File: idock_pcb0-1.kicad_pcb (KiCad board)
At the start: 2 copper layers, 8 parts, among them J1 entrada, U1 ATmega32A-PU, Y1 8mhz

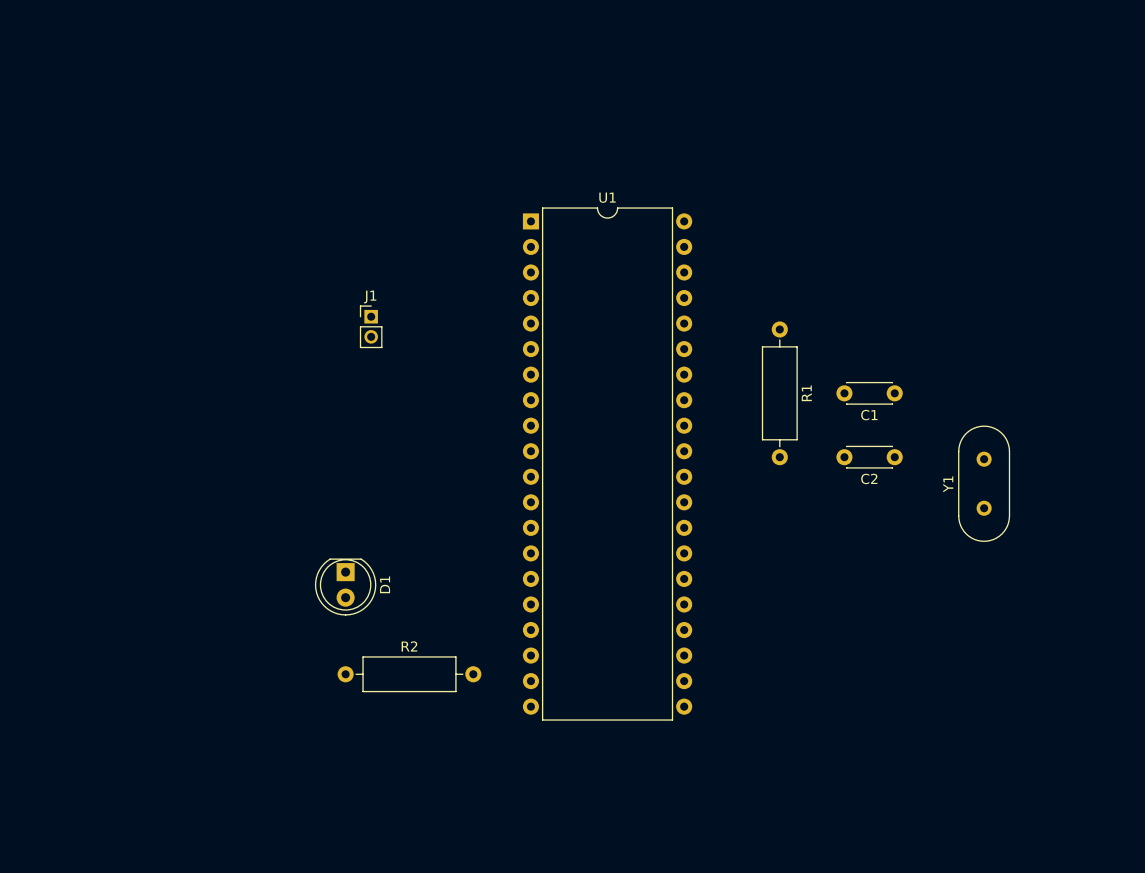
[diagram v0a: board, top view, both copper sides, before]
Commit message: add conections to ipod pcb
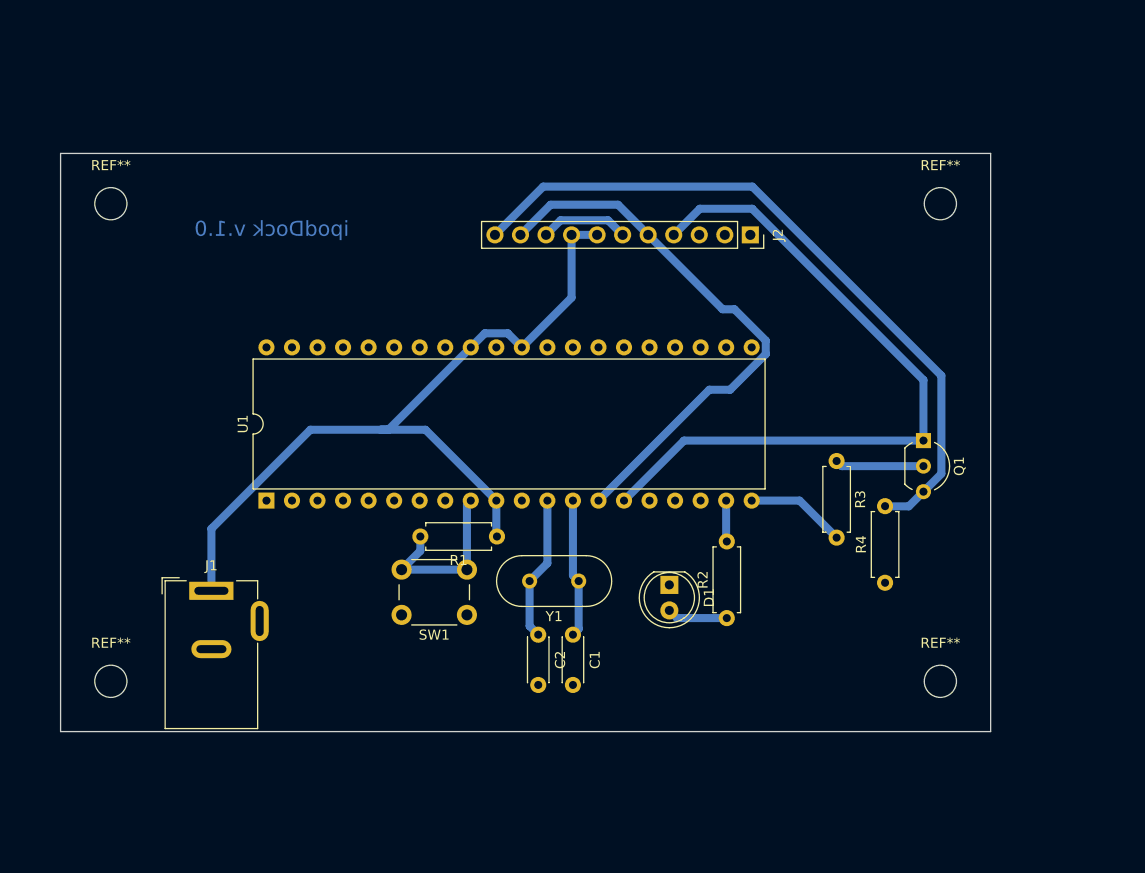
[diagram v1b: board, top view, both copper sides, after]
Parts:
- added J2: bluetooth-dock, Connector_PinSocket_2.54mm:PinSocket_1x11_P2.54mm_Vertical, F.Cu at (173.6, 70.6)
- added Q1: BC548, Package_TO_SOT_THT:TO-92_Inline_Wide, F.Cu at (190.8, 91.1)
- added R3: 10k, Resistor_THT:R_Axial_DIN0207_L6.3mm_D2.5mm_P7.62mm_Horizontal, F.Cu at (182.2, 93.1)
- added R4: 47k, Resistor_THT:R_Axial_DIN0207_L6.3mm_D2.5mm_P7.62mm_Horizontal, F.Cu at (187.0, 105.2)
- added REF**: MountingHole_3.2mm_M3_DIN965, MountingHole:MountingHole_3.2mm_M3_DIN965, F.Cu at (110.0, 115.0)
- added REF**: MountingHole_3.2mm_M3_DIN965, MountingHole:MountingHole_3.2mm_M3_DIN965, F.Cu at (192.5, 115.0)
- added REF**: MountingHole_3.2mm_M3_DIN965, MountingHole:MountingHole_3.2mm_M3_DIN965, F.Cu at (192.5, 67.5)
- added REF**: MountingHole_3.2mm_M3_DIN965, MountingHole:MountingHole_3.2mm_M3_DIN965, F.Cu at (110.0, 67.5)
- added SW1: Reset, Button_Switch_THT:SW_PUSH_6mm, F.Cu at (145.4, 108.4)
- J1: value entrada -> Barrel_Jack_Switch; footprint Connector_PinHeader_2.00mm:PinHeader_1x02_P2.00mm_Vertical -> Connector_BarrelJack:BarrelJack_Wuerth_6941xx301002
- R1, R2: footprint Resistor_THT:R_Axial_DIN0309_L9.0mm_D3.2mm_P12.70mm_Horizontal -> Resistor_THT:R_Axial_DIN0207_L6.3mm_D2.5mm_P7.62mm_Horizontal
- moved Y1 41.0 mm to (156.5, 105.0), turned to 180 degrees
- moved C1 40.0 mm to (156.0, 110.4), turned to 270 degrees
- moved C2 39.6 mm to (152.5, 110.4), turned to 270 degrees
- moved R2 38.3 mm to (171.3, 108.7), turned to 90 degrees
- moved U1 38.2 mm to (125.5, 97.0), turned to 90 degrees
- moved R1 34.9 mm to (148.4, 100.6), turned to 180 degrees
- moved D1 32.2 mm to (165.5, 105.4)
- moved J1 31.6 mm to (120.0, 106.0)
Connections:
- J1 pad 1: GND -> +5V
- J1 pad 2: +5V -> GND
- R1 pad 2: GND -> Net-(R1-Pad2)
- U1 pad 9: GND -> Net-(R1-Pad2)
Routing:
- net +5V: track 0.00 -> 80.2 mm
- net Net-(J2-Pad4): track 0.00 -> 71.2 mm
- net Net-(J2-Pad11): track 0.00 -> 70.9 mm
- net Net-(J2-Pad10): track 0.00 -> 55.3 mm
- net Net-(R1-Pad2): track 0.00 -> 17.6 mm
- net Net-(C2-Pad1): track 0.00 -> 14.4 mm
- net Net-(C1-Pad1): track 0.00 -> 13.8 mm
- net Net-(R3-Pad2): track 0.00 -> 9.97 mm
- net Net-(Q1-Pad2): track 0.00 -> 8.85 mm
- net GND: track 0.00 -> 8.82 mm
- net Net-(D1-Pad2): track 0.00 -> 6.03 mm
- net Net-(R2-Pad2): track 0.00 -> 4.09 mm
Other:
- board outline added: 92.5 x 57.5 mm
- board text added: "audio-out"
- board text added: "ipodDock v.1.0"

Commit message: add labels to PCB
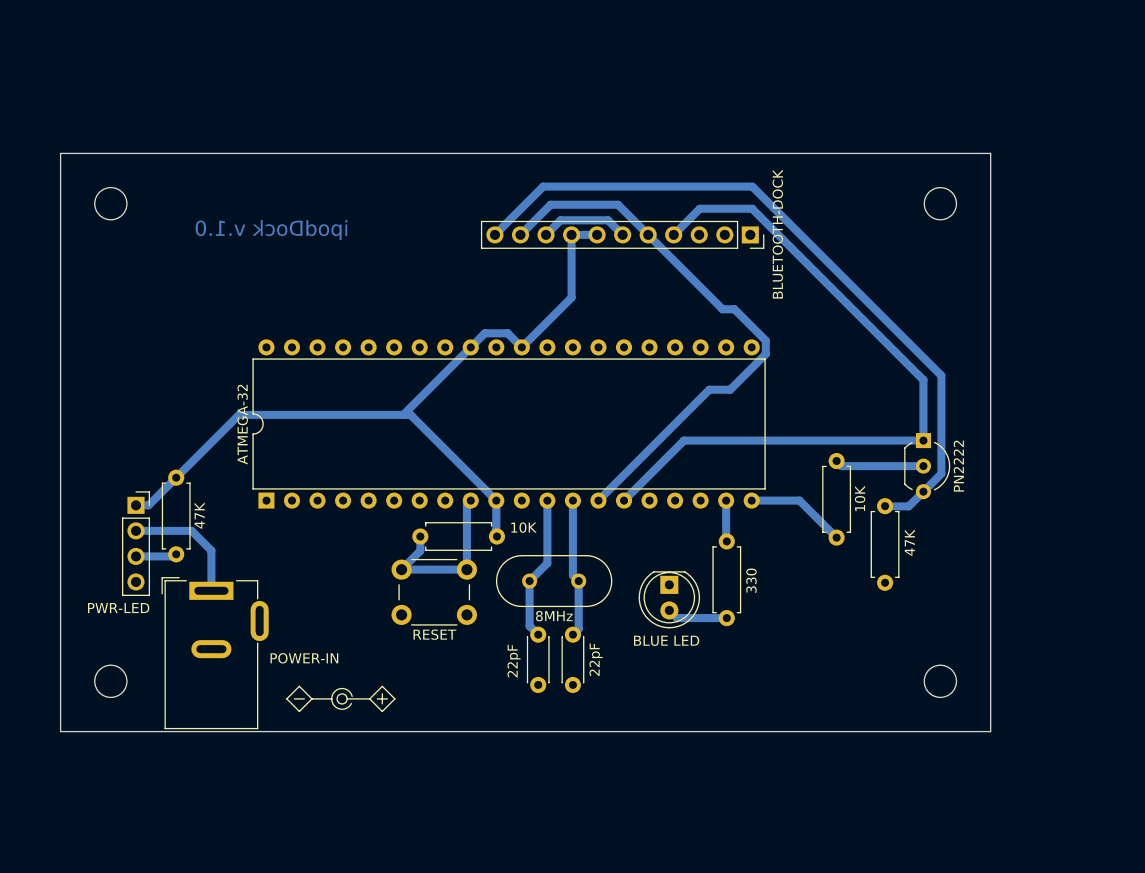
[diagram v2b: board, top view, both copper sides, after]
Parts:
- removed R3: 10k, Resistor_THT:R_Axial_DIN0207_L6.3mm_D2.5mm_P7.62mm_Horizontal
- removed U1: ATmega32A-PU, Package_DIP:DIP-40_W15.24mm
- removed Y1: 8mhz, Crystal:Crystal_HC49-4H_Vertical
- added 10K: 10k, Resistor_THT:R_Axial_DIN0207_L6.3mm_D2.5mm_P7.62mm_Horizontal, F.Cu at (182.2, 93.1)
- added 47K: 47k, Resistor_THT:R_Axial_DIN0207_L6.3mm_D2.5mm_P7.62mm_Horizontal, F.Cu at (116.5, 94.8)
- added 8MHz: 8mhz, Crystal:Crystal_HC49-4H_Vertical, F.Cu at (156.5, 105.0)
- added ATMEGA-32: ATmega32A-PU, Package_DIP:DIP-40_W15.24mm, F.Cu at (125.5, 97.0)
- added PWR-LED: POWERLED, Connector_PinSocket_2.54mm:PinSocket_1x04_P2.54mm_Vertical, F.Cu at (112.5, 97.5)
- BLUE LED: renamed from D1
- renumbered R1 to 10K, C2 to 22pF, C1 to 22pF, R2 to 330, R4 to 47K, J2 to BLUETOOTH-DOCK, Q1 to PN2222, J1 to POWER-IN, SW1 to RESET
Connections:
- POWER-IN pad 1: +5V -> Net-(J1-Pad1)
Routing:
- net Net-(J1-Pad1): track 0.00 -> 12.3 mm
- net Net-(J3-Pad3): track 0.00 -> 4.09 mm
- net +5V: track 80.2 -> 78.2 mm

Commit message: update Fsilk pinout
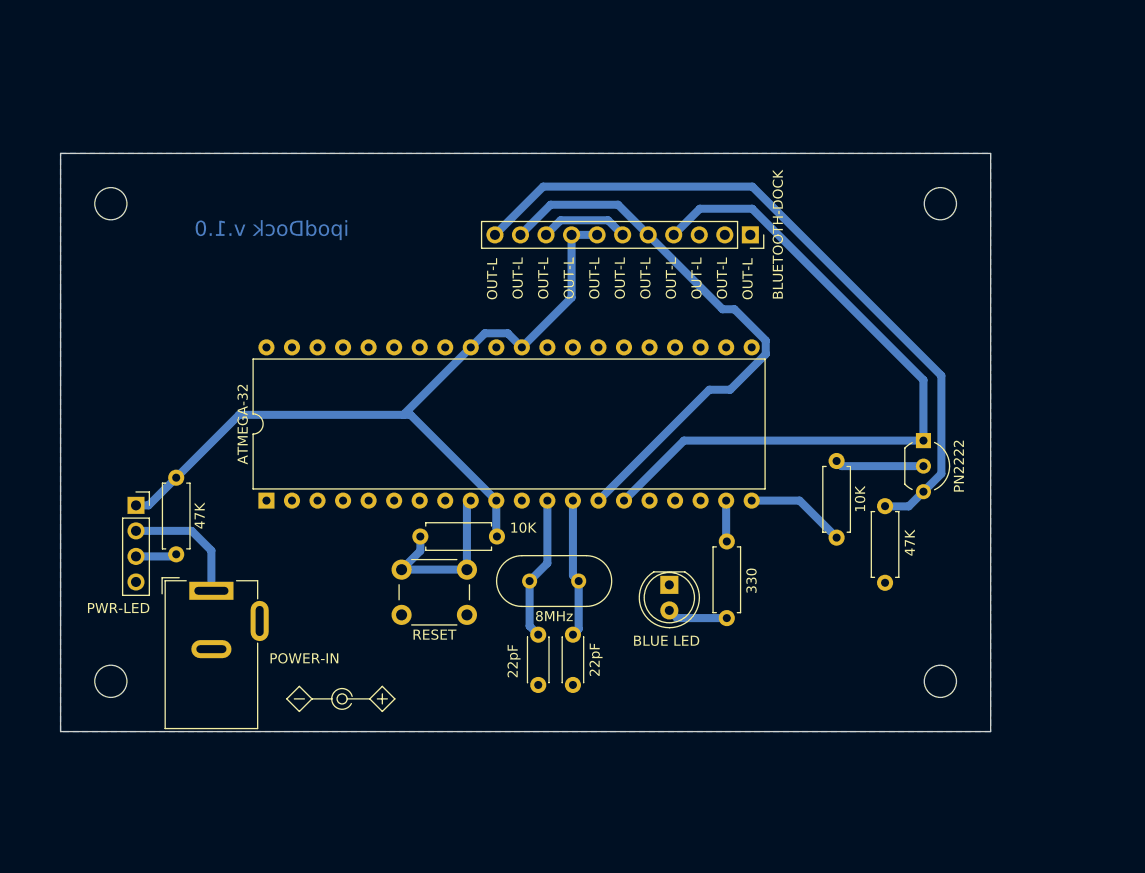
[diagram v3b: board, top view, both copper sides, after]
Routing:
- added copper zone on B.Cu, net GND
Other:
- board text added: "OUT-L"
- board text removed: "audio-out"

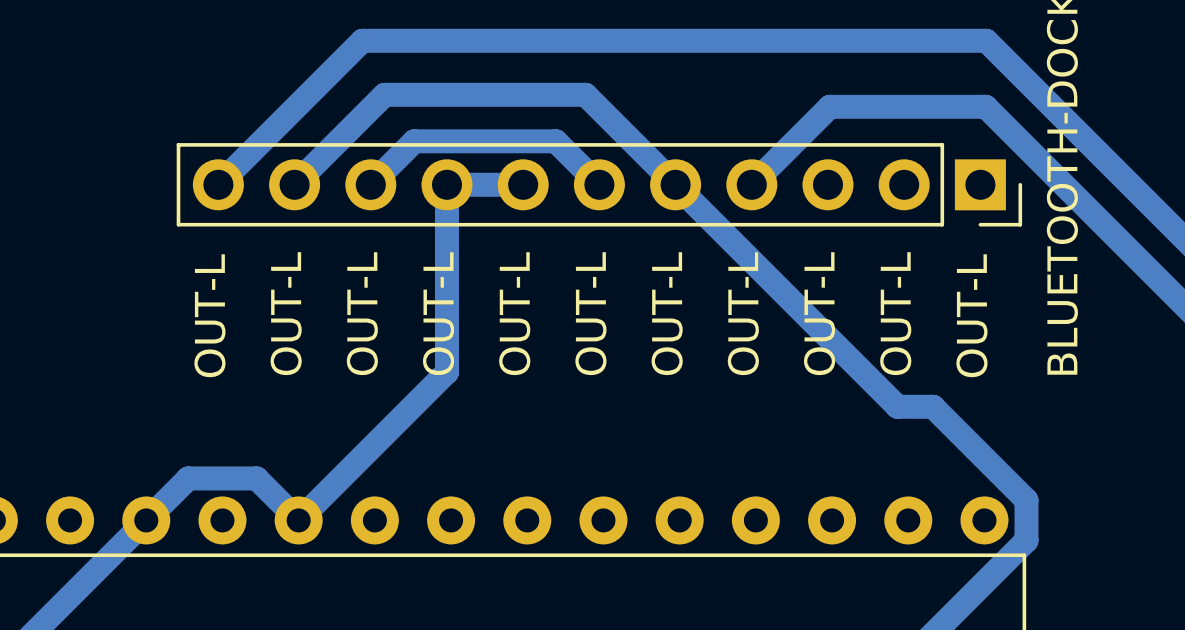
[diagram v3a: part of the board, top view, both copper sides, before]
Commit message: add real connections on PCB outport
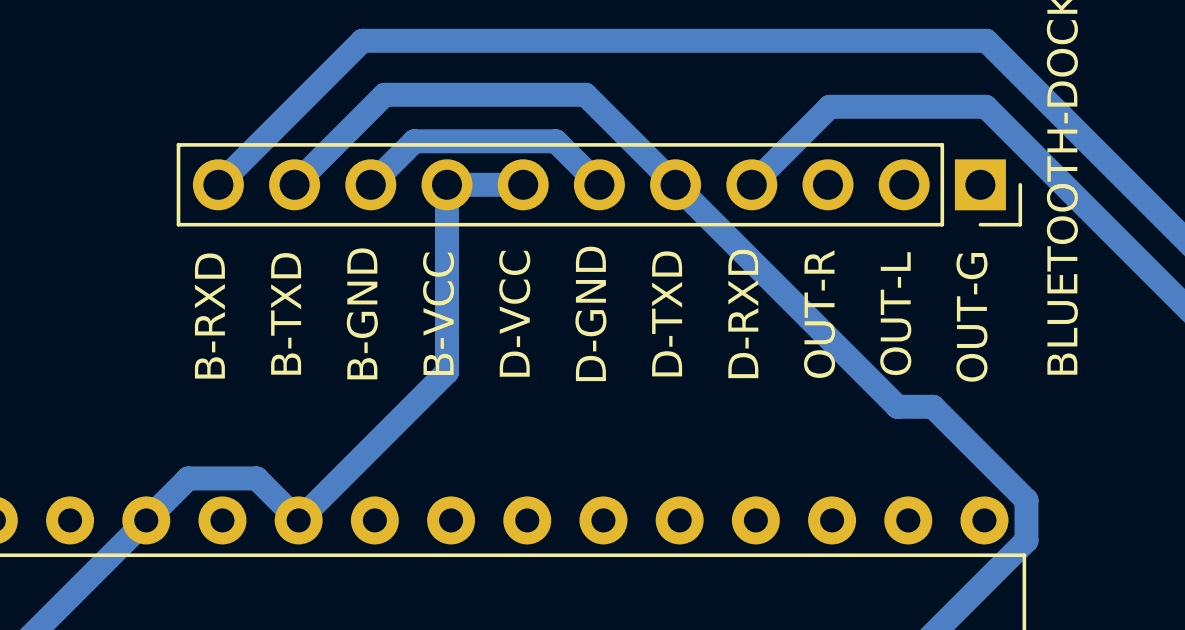
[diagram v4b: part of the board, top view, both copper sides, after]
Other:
- board text added: "B-GND"
- board text added: "B-RXD"
- board text added: "B-TXD"
- board text added: "B-VCC"
- board text added: "D-GND"
- board text added: "D-RXD"
- board text added: "D-TXD"
- board text added: "D-VCC"
- board text added: "OUT-G"
- board text added: "OUT-R"
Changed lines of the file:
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@@
     )
   )
-  (gr_text OUT-L (at 147.955 75 90) (layer F.SilkS)
+  (gr_text D-TXD (at 163.195 74.93 90) (layer F.SilkS)
     (effects (font (size 1 1) (thickness 0.15)))
   )
-  (gr_text OUT-L (at 150.495 74.93 90) (layer F.SilkS)
+  (gr_text B-RXD (at 147.955 75 90) (layer F.SilkS)
     (effects (font (size 1 1) (thickness 0.15)))
   )
-  (gr_text OUT-L (at 153.035 74.93 90) (layer F.SilkS)
+  (gr_text B-TXD (at 150.495 74.93 90) (layer F.SilkS)
     (effects (font (size 1 1) (thickness 0.15)))
   )
-  (gr_text OUT-L (at 155.575 74.93 90) (layer F.SilkS)
+  (gr_text B-GND (at 153.035 74.93 90) (layer F.SilkS)
     (effects (font (size 1 1) (thickness 0.15)))
   )
-  (gr_text OUT-L (at 158.115 74.93 90) (layer F.SilkS)
+  (gr_text B-VCC (at 155.575 74.93 90) (layer F.SilkS)
     (effects (font (size 1 1) (thickness 0.15)))
   )
-  (gr_text OUT-L (at 160.655 74.93 90) (layer F.SilkS)
+  (gr_text D-VCC (at 158.115 74.93 90) (layer F.SilkS)
     (effects (font (size 1 1) (thickness 0.15)))
   )
-  (gr_text OUT-L (at 163.195 74.93 90) (layer F.SilkS)
+  (gr_text D-GND (at 160.655 74.93 90) (layer F.SilkS)
     (effects (font (size 1 1) (thickness 0.15)))
   )
-  (gr_text OUT-L (at 165.735 74.93 90) (layer F.SilkS)
+  (gr_text D-RXD (at 165.735 74.93 90) (layer F.SilkS)
     (effects (font (size 1 1) (thickness 0.15)))
   )
-  (gr_text OUT-L (at 168.275 74.93 90) (layer F.SilkS)
+  (gr_text OUT-R (at 168.275 74.93 90) (layer F.SilkS)
     (effects (font (size 1 1) (thickness 0.15)))
   )
@@
     (effects (font (size 1 1) (thickness 0.15)))
   )
-  (gr_text OUT-L (at 173.355 75 90) (layer F.SilkS)
+  (gr_text OUT-G (at 173.355 75 90) (layer F.SilkS)
     (effects (font (size 1 1) (thickness 0.15)))
   )

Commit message: retomando PCB
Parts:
- D1: renamed from BLUE LED; value LED BLUE -> LED BLUE DATA RX
- renumbered 22pF to C1, 22pF to C2, POWER-IN to J1, BLUETOOTH-DOCK to J2, PWR-LED to J3, PN2222 to Q1, 10K to R1, 330 to R2, 10K to R3, 47K to R4, 47K to R5, RESET to SW1, ATMEGA-32 to U1, 8MHz to Y1
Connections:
- J3 pad 1: +5V -> Net-(J1-Pad1)
- J3 pad 2: Net-(J1-Pad1) -> +5V

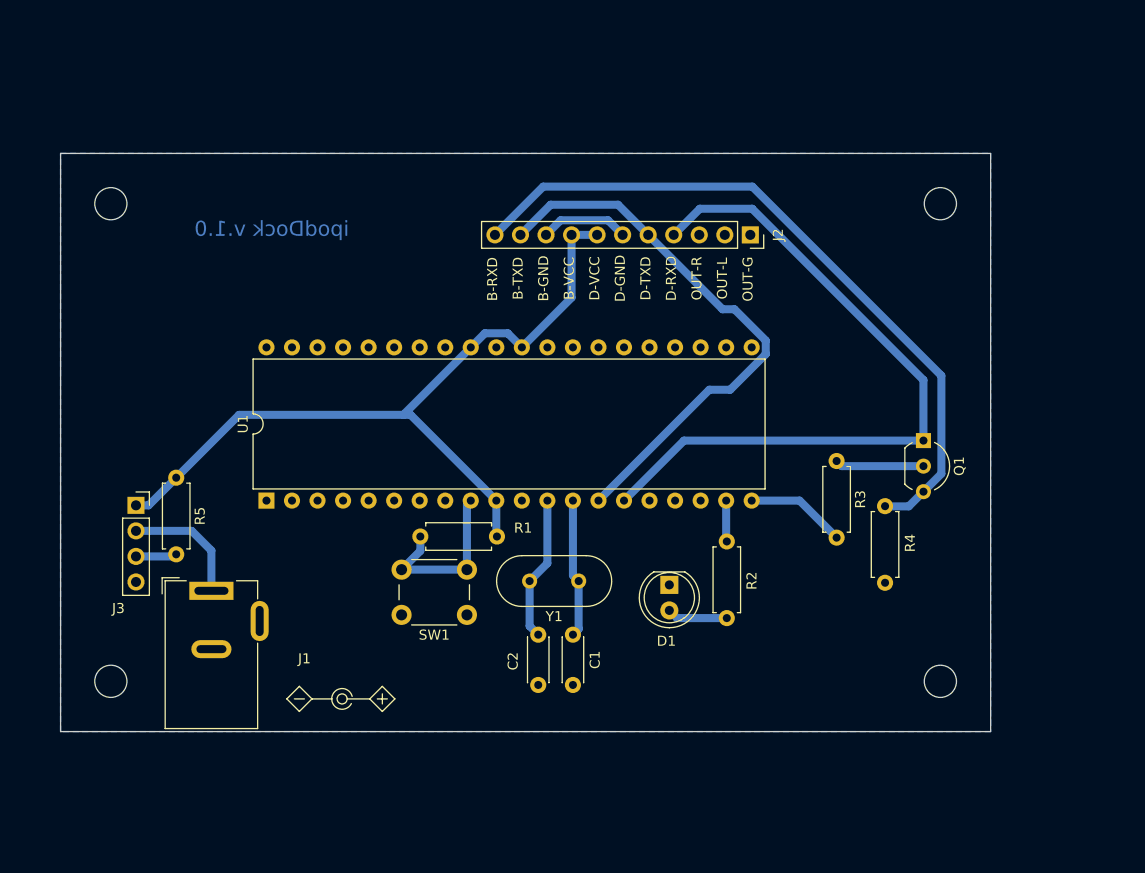
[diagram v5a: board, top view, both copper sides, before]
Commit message: pcb with correct size and holes
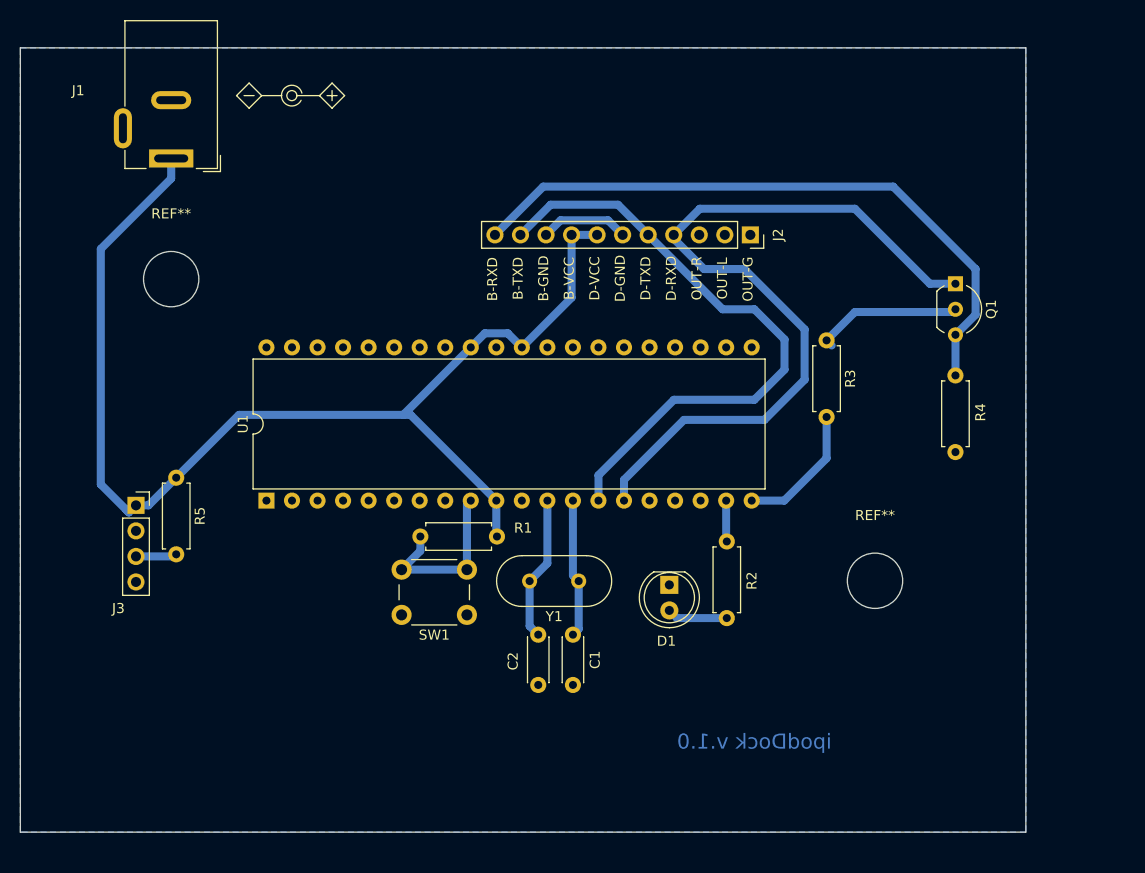
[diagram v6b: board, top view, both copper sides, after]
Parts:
- removed the REF** at (110.0, 115.0)
- removed the REF** at (192.5, 115.0)
- removed the REF** at (192.5, 67.5)
- removed the REF** at (110.0, 67.5)
- added REF**: MountingHole_5.5mm, MountingHole:MountingHole_5.5mm, F.Cu at (116.0, 75.0)
- added REF**: MountingHole_5.5mm, MountingHole:MountingHole_5.5mm, F.Cu at (186.0, 105.0)
- moved J1 43.2 mm to (116.0, 63.0), turned to 180 degrees
- moved Q1 15.9 mm to (194.0, 75.5)
- moved R4 14.8 mm to (194.0, 92.2)
- moved R3 12.0 mm to (181.2, 81.1)
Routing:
- net Net-(J1-Pad1): track 12.3 -> 39.7 mm
- net Net-(J2-Pad4): track 71.2 -> 78.5 mm
- net Net-(J2-Pad11): track 70.9 -> 64.6 mm
- net Net-(J2-Pad10): track 55.3 -> 61.4 mm
- net Net-(Q1-Pad2): track 8.85 -> 14.8 mm
- net Net-(R3-Pad2): track 9.97 -> 13.3 mm
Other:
- board size 92.5 x 57.5 mm -> 100 x 78 mm

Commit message: add footprints PJRAN2X1UO2
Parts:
- added J4: PJRAN2X1U02, footprints:SWITCHCRAFT_PJRAN2X1U02, F.Cu at (149.0, 58.0)
